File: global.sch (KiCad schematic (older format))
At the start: 37 parts, among them Q101 MMBT3904, U101 74HCT125, U102 74HC595, U103 74HC595, U104 74HC595, U105 74HC165

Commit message: renumbered pcb
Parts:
- renumbered C102 to C44, C103 to C45, C104 to C46, C105 to C50, C101 to C6, ENC101 to ENC1, JP101 to JP1, JP103 to JP2, JP102 to JP3, Q101 to Q5, R116 to R10, R117 to R11, R122 to R34, R105 to R47, R101 to R48, R102 to R53, R103 to R56, R104 to R59, R120 to R64, R118 to R65, R121 to R67, R113 to R68, R112 to R69, R119 to R7, R111 to R70, R110 to R71, R109 to R72, R108 to R73, R107 to R74, R106 to R75, R114 to R8, R115 to R9, U105 to U11, U102 to U12, U103 to U13, U104 to U14, U101 to U5
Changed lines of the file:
@@
 $EndDescr
 $Comp
-L ALPS-STEC12E08 ENC101
+L ALPS-STEC12E08 ENC1
 U 1 1 59AC9C93
 P 3050 6850
-F 0 "ENC101" H 3050 6500 50  0000 C CNN
+F 0 "ENC1" H 3050 6500 50  0000 C CNN
 F 1 "ALPS-STEC12E08" H 3050 7200 50  0000 C CNN
 F 2 "w_rotary_encoder:ALPS_STEC12E08" H 3050 6850 60  0001 C CNN
@@
 $EndComp
 $Comp
-L 74HC165 U105
+L 74HC165 U11
 U 1 1 59D8CB67
 P 5500 5100
-F 0 "U105" H 6000 4250 60  0000 C CNN
+F 0 "U11" H 6000 4250 60  0000 C CNN
 F 1 "74HC165" H 6000 5250 60  0000 C CNN
 F 2 "Housings_SOIC:SOIC-16_3.9x9.9mm_Pitch1.27mm" H 5500 5100 60  0001 C CNN
@@
 $EndComp
 $Comp
-L 74HC595 U102
+L 74HC595 U12
 U 1 1 59D8CB9A
 P 5500 900
-F 0 "U102" H 6000 50  60  0000 C CNN
+F 0 "U12" H 6000 50  60  0000 C CNN
 F 1 "74HC595" H 6000 1050 60  0000 C CNN
 F 2 "Housings_SOIC:SOIC-16_3.9x9.9mm_Pitch1.27mm" H 5500 900 60  0001 C CNN
@@
 $EndComp
 $Comp
-L 74HC595 U103
+L 74HC595 U13
 U 1 1 59DABD8B
 P 5500 2300
-F 0 "U103" H 6000 1450 60  0000 C CNN
+F 0 "U13" H 6000 1450 60  0000 C CNN
 F 1 "74HC595" H 6000 2450 60  0000 C CNN
 F 2 "Housings_SOIC:SOIC-16_3.9x9.9mm_Pitch1.27mm" H 5500 2300 60  0001 C CNN
@@
 $EndComp
 $Comp
-L 74HC595 U104
+L 74HC595 U14
 U 1 1 59DABDC7
 P 5500 3700
-F 0 "U104" H 6000 2850 60  0000 C CNN
+F 0 "U14" H 6000 2850 60  0000 C CNN
 F 1 "74HC595" H 6000 3850 60  0000 C CNN
 F 2 "Housings_SOIC:SOIC-16_3.9x9.9mm_Pitch1.27mm" H 5500 3700 60  0001 C CNN
@@
 $EndComp
 $Comp
-L C C101
+L C C6
 U 1 1 59DAD327
 P 5000 6850
-F 0 "C101" H 5025 6950 50  0000 L CNN
+F 0 "C6" H 5025 6950 50  0000 L CNN
 F 1 "100n" H 5025 6750 50  0000 L CNN
 F 2 "w_capacitor:C_0603" H 5038 6700 50  0001 C CNN
@@
 $EndComp
 $Comp
-L C C102
+L C C44
 U 1 1 59DAD399
 P 5300 6850
-F 0 "C102" H 5325 6950 50  0000 L CNN
+F 0 "C44" H 5325 6950 50  0000 L CNN
 F 1 "100n" H 5325 6750 50  0000 L CNN
 F 2 "w_capacitor:C_0603" H 5338 6700 50  0001 C CNN
@@
 $EndComp
 $Comp
-L C C103
+L C C45
 U 1 1 59DAD3D5
 P 5600 6850
-F 0 "C103" H 5625 6950 50  0000 L CNN
+F 0 "C45" H 5625 6950 50  0000 L CNN
 F 1 "100n" H 5625 6750 50  0000 L CNN
 F 2 "w_capacitor:C_0603" H 5638 6700 50  0001 C CNN
@@
 $EndComp
 $Comp
-L C C104
+L C C46
 U 1 1 59DAD3DB
 P 5900 6850
-F 0 "C104" H 5925 6950 50  0000 L CNN
+F 0 "C46" H 5925 6950 50  0000 L CNN
 F 1 "100n" H 5925 6750 50  0000 L CNN
 F 2 "w_capacitor:C_0603" H 5938 6700 50  0001 C CNN
@@
 $EndComp
 $Comp
-L C C105
+L C C50
 U 1 1 59DB526D
 P 6200 6850
-F 0 "C105" H 6225 6950 50  0000 L CNN
+F 0 "C50" H 6225 6950 50  0000 L CNN
 F 1 "100n" H 6225 6750 50  0000 L CNN
 F 2 "w_capacitor:C_0603" H 6238 6700 50  0001 C CNN
@@
 $EndComp
 $Comp
-L NHD-3.12-25664UC JP102
+L NHD-3.12-25664UC JP3
 U 1 1 59DBF1B1
 P 3000 3800
-F 0 "JP102" H 3650 1750 60  0000 C CNN
+F 0 "JP3" H 3650 1750 60  0000 C CNN
 F 1 "NHD-3.12-25664UC" H 3650 3950 60  0000 C CNN
 F 2 "w_lcd:NHD-3.12-25664UC" H 3200 4000 60  0001 C CNN
@@
 $EndComp
 $Comp
-L Micro_SD_Card JP103
+L Micro_SD_Card JP2
 U 1 1 59DC0C9C
 P 10100 1600
-F 0 "JP103" H 9450 2200 50  0000 C CNN
+F 0 "JP2" H 9450 2200 50  0000 C CNN
 F 1 "PJS008U-3000" H 10750 2200 50  0000 R CNN
 F 2 "w_connector:PJS008U-3000-0" H 11250 1900 50  0001 C CNN
@@
 $EndComp
 $Comp
-L USB_A JP101
+L USB_A JP1
 U 1 1 59DE5EB2
 P 10000 5600
-F 0 "JP101" H 9800 6050 50  0000 L CNN
+F 0 "JP1" H 9800 6050 50  0000 L CNN
 F 1 "USB_A" H 9800 5950 50  0000 L CNN
 F 2 "w_connector:MOLEX_USB_105057" H 10150 5550 50  0001 C CNN
@@
 $EndComp
 $Comp
-L R R101
+L R R48
 U 1 1 59E55F0E
 P 6700 4950
-F 0 "R101" V 6650 5100 50  0000 L CNN
+F 0 "R48" V 6650 5100 50  0000 L CNN
 F 1 "10k" V 6700 4950 50  0000 C CNN
 F 2 "w_resistor:R_0603" V 6630 4950 50  0001 C CNN
@@
 $EndComp
 $Comp
-L R R102
+L R R53
 U 1 1 59E560D3
 P 6800 4950
-F 0 "R102" V 6750 5100 50  0000 L CNN
+F 0 "R53" V 6750 5100 50  0000 L CNN
 F 1 "10k" V 6800 4950 50  0000 C CNN
 F 2 "w_resistor:R_0603" V 6730 4950 50  0001 C CNN
@@
 $EndComp
 $Comp
-L R R103
+L R R56
 U 1 1 59E56118
 P 6900 4950
-F 0 "R103" V 6850 5100 50  0000 L CNN
+F 0 "R56" V 6850 5100 50  0000 L CNN
 F 1 "10k" V 6900 4950 50  0000 C CNN
 F 2 "w_resistor:R_0603" V 6830 4950 50  0001 C CNN
@@
 $EndComp
 $Comp
-L R R104
+L R R59
 U 1 1 59E56160
 P 7000 4950
-F 0 "R104" V 6950 5100 50  0000 L CNN
+F 0 "R59" V 6950 5100 50  0000 L CNN
 F 1 "10k" V 7000 4950 50  0000 C CNN
 F 2 "w_resistor:R_0603" V 6930 4950 50  0001 C CNN
@@
 $EndComp
 $Comp
-L R R105
+L R R47
 U 1 1 59E561AB
 P 7100 4950
-F 0 "R105" V 7050 5100 50  0000 L CNN
+F 0 "R47" V 7050 5100 50  0000 L CNN
 F 1 "10k" V 7100 4950 50  0000 C CNN
 F 2 "w_resistor:R_0603" V 7030 4950 50  0001 C CNN
@@
 $EndComp
 $Comp
-L R R107
+L R R74
 U 1 1 59E604C8
 P 6750 2400
-F 0 "R107" V 6700 2550 50  0000 L CNN
+F 0 "R74" V 6700 2550 50  0000 L CNN
 F 1 "470" V 6750 2400 50  0000 C CNN
 F 2 "w_resistor:R_0603" V 6680 2400 50  0001 C CNN
@@
 $EndComp
 $Comp
-L R R106
+L R R75
 U 1 1 59E60528
 P 6750 2300
-F 0 "R106" V 6700 2450 50  0000 L CNN
+F 0 "R75" V 6700 2450 50  0000 L CNN
 F 1 "470" V 6750 2300 50  0000 C CNN
 F 2 "w_resistor:R_0603" V 6680 2300 50  0001 C CNN
@@
 $EndComp
 $Comp
-L R R108
+L R R73
 U 1 1 59E60C94
 P 6750 2500
-F 0 "R108" V 6700 2650 50  0000 L CNN
+F 0 "R73" V 6700 2650 50  0000 L CNN
 F 1 "470" V 6750 2500 50  0000 C CNN
 F 2 "w_resistor:R_0603" V 6680 2500 50  0001 C CNN
@@
 $EndComp
 $Comp
-L R R109
+L R R72
 U 1 1 59E60F5A
 P 6750 2600
-F 0 "R109" V 6700 2750 50  0000 L CNN
+F 0 "R72" V 6700 2750 50  0000 L CNN
 F 1 "470" V 6750 2600 50  0000 C CNN
 F 2 "w_resistor:R_0603" V 6680 2600 50  0001 C CNN
@@
 $EndComp
 $Comp
-L R R113
+L R R68
 U 1 1 59E61471
 P 6750 3000
-F 0 "R113" V 6700 3150 50  0000 L CNN
+F 0 "R68" V 6700 3150 50  0000 L CNN
 F 1 "470" V 6750 3000 50  0000 C CNN
 F 2 "w_resistor:R_0603" V 6680 3000 50  0001 C CNN
@@
 $EndComp
 $Comp
-L R R112
+L R R69
 U 1 1 59E6153A
 P 6750 2900
-F 0 "R112" V 6700 3050 50  0000 L CNN
+F 0 "R69" V 6700 3050 50  0000 L CNN
 F 1 "470" V 6750 2900 50  0000 C CNN
 F 2 "w_resistor:R_0603" V 6680 2900 50  0001 C CNN
@@
 $EndComp
 $Comp
-L R R111
+L R R70
 U 1 1 59E61584
 P 6750 2800
-F 0 "R111" V 6700 2950 50  0000 L CNN
+F 0 "R70" V 6700 2950 50  0000 L CNN
 F 1 "470" V 6750 2800 50  0000 C CNN
 F 2 "w_resistor:R_0603" V 6680 2800 50  0001 C CNN
@@
 $EndComp
 $Comp
-L R R110
+L R R71
 U 1 1 59E6158A
 P 6750 2700
-F 0 "R110" V 6700 2850 50  0000 L CNN
+F 0 "R71" V 6700 2850 50  0000 L CNN
 F 1 "470" V 6750 2700 50  0000 C CNN
 F 2 "w_resistor:R_0603" V 6680 2700 50  0001 C CNN
@@
 $EndComp
 $Comp
-L 74HCT125 U101
+L 74HCT125 U5
 U 1 1 59E5EC51
 P 3000 800
-F 0 "U101" H 3500 -250 60  0000 C CNN
+F 0 "U5" H 3500 -250 60  0000 C CNN
 F 1 "74HCT125" H 3500 950 60  0000 C CNN
 F 2 "Housings_SOIC:SOIC-14_3.9x8.7mm_Pitch1.27mm" H 3450 900 60  0001 C CNN
@@
 $EndComp
 $Comp
-L R R117
+L R R11
 U 1 1 5AEA4C2A
 P 8900 1050
-F 0 "R117" V 8980 1050 50  0000 C CNN
+F 0 "R11" V 8980 1050 50  0000 C CNN
 F 1 "33k" V 8900 1050 50  0000 C CNN
 F 2 "w_resistor:R_0603" V 8830 1050 50  0001 C CNN
@@
 $EndComp
 $Comp
-L R R119
+L R R7
 U 1 1 5AEA4CDA
 P 8900 2250
-F 0 "R119" V 8980 2250 50  0000 C CNN
+F 0 "R7" V 8980 2250 50  0000 C CNN
 F 1 "1M" V 8900 2250 50  0000 C CNN
 F 2 "w_resistor:R_0603" V 8830 2250 50  0001 C CNN
@@
 $EndComp
 $Comp
-L R R114
+L R R8
 U 1 1 5AEA4D5E
 P 8300 1050
-F 0 "R114" V 8380 1050 50  0000 C CNN
+F 0 "R8" V 8380 1050 50  0000 C CNN
 F 1 "33k" V 8300 1050 50  0000 C CNN
 F 2 "w_resistor:R_0603" V 8230 1050 50  0001 C CNN
@@
 $EndComp
 $Comp
-L R R115
+L R R9
 U 1 1 5AEA4DC8
 P 8500 1050
-F 0 "R115" V 8580 1050 50  0000 C CNN
+F 0 "R9" V 8580 1050 50  0000 C CNN
 F 1 "33k" V 8500 1050 50  0000 C CNN
 F 2 "w_resistor:R_0603" V 8430 1050 50  0001 C CNN
@@
 $EndComp
 $Comp
-L R R116
+L R R10
 U 1 1 5AEA93F2
 P 8700 1050
-F 0 "R116" V 8780 1050 50  0000 C CNN
+F 0 "R10" V 8780 1050 50  0000 C CNN
 F 1 "33k" V 8700 1050 50  0000 C CNN
 F 2 "w_resistor:R_0603" V 8630 1050 50  0001 C CNN
@@
 $EndComp
 $Comp
-L R R122
+L R R34
 U 1 1 5AEB2AD1
 P 2700 5650
-F 0 "R122" V 2780 5650 50  0000 C CNN
+F 0 "R34" V 2780 5650 50  0000 C CNN
 F 1 "10k" V 2700 5650 50  0000 C CNN
 F 2 "w_resistor:R_0603" V 2630 5650 50  0001 C CNN
@@
 $EndComp
 $Comp
-L MMBT3904 Q101
+L MMBT3904 Q5
 U 1 1 5AEB9A70
 P 4000 2700
-F 0 "Q101" H 4200 2775 50  0000 L CNN
+F 0 "Q5" H 4200 2775 50  0000 L CNN
 F 1 "MMBT3904" H 4200 2700 50  0000 L CNN
 F 2 "TO_SOT_Packages_SMD:SOT-23" H 4200 2625 50  0001 L CIN
@@
 $EndComp
 $Comp
-L R R118
+L R R65
 U 1 1 5AEB9A79
 P 4100 2150
-F 0 "R118" V 4180 2150 50  0000 C CNN
+F 0 "R65" V 4180 2150 50  0000 C CNN
 F 1 "1k" V 4100 2150 50  0000 C CNN
 F 2 "w_resistor:R_0603" V 4030 2150 50  0001 C CNN
@@
 $EndComp
 $Comp
-L R R120
+L R R64
 U 1 1 5AEBCC66
 P 3450 2700
-F 0 "R120" V 3530 2700 50  0000 C CNN
+F 0 "R64" V 3530 2700 50  0000 C CNN
 F 1 "10k" V 3450 2700 50  0000 C CNN
 F 2 "w_resistor:R_0603" V 3380 2700 50  0001 C CNN
@@
 $EndComp
 $Comp
-L R R121
+L R R67
 U 1 1 5AEBCE61
 P 3700 2950
-F 0 "R121" V 3780 2950 50  0000 C CNN
+F 0 "R67" V 3780 2950 50  0000 C CNN
 F 1 "100k" V 3700 2950 50  0000 C CNN
 F 2 "w_resistor:R_0603" V 3630 2950 50  0001 C CNN

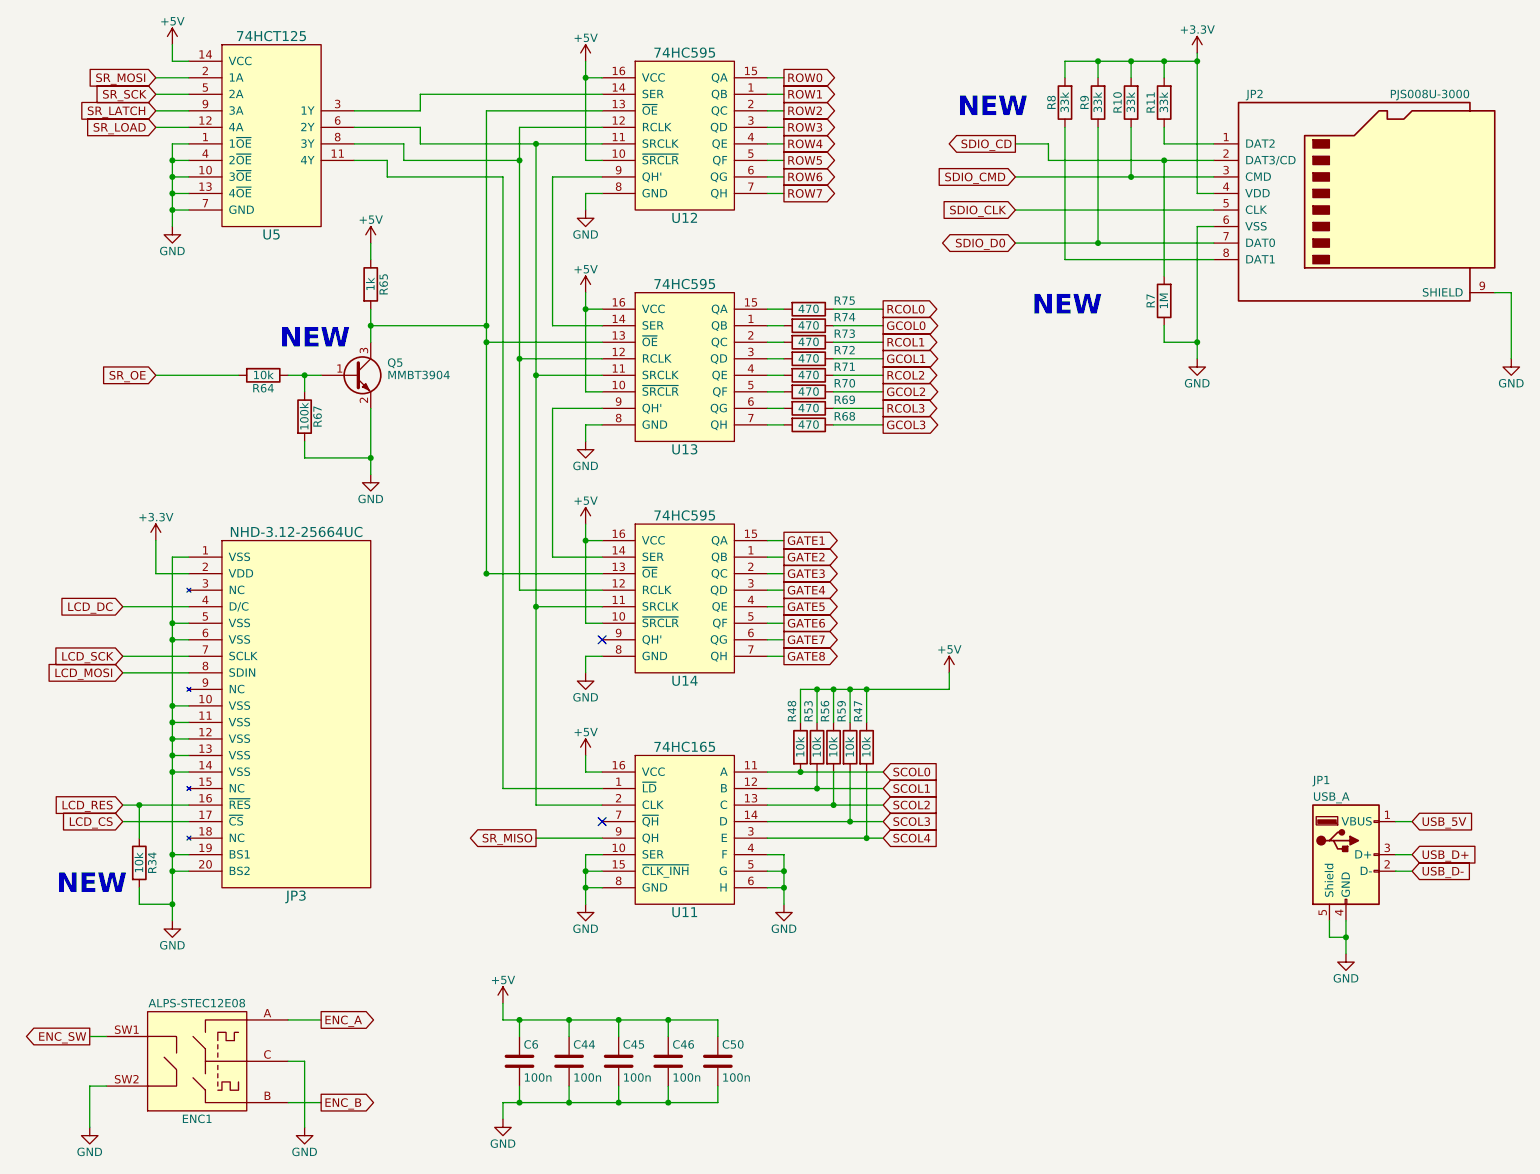
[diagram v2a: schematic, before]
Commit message: corrected some part values
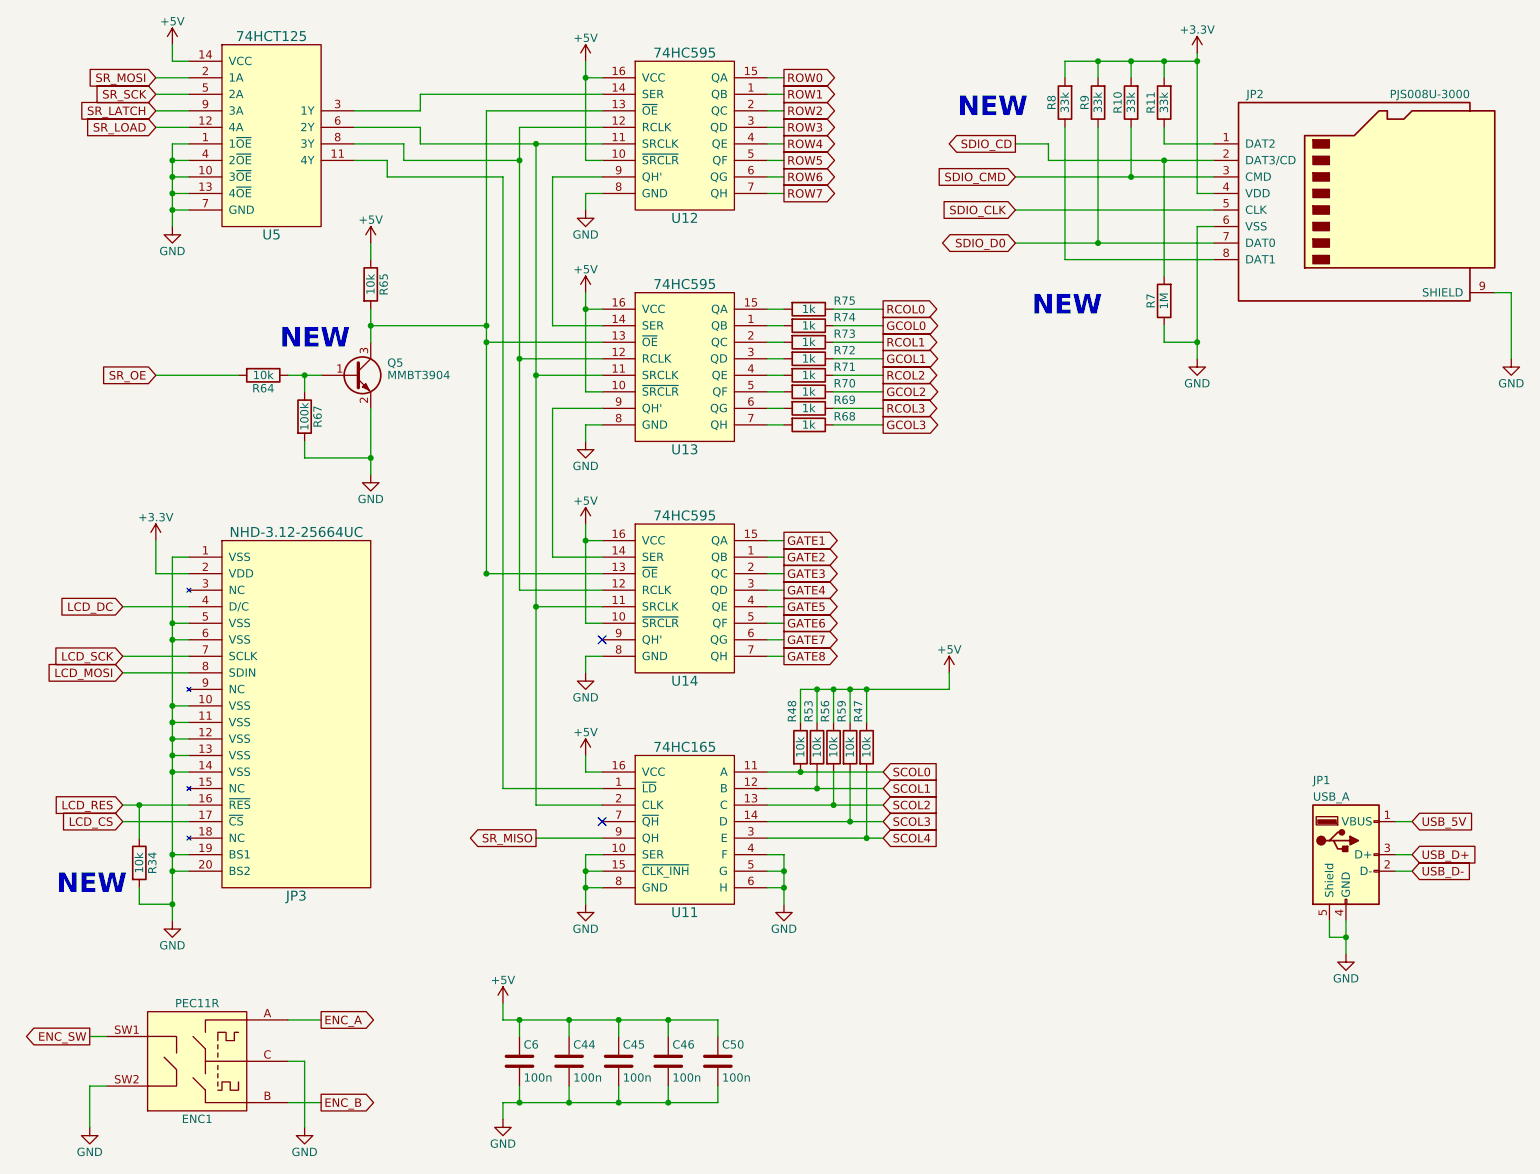
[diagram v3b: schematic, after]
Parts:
- ENC1: value ALPS-STEC12E08 -> PEC11R; MFP PEC11R-4225F-S0024 -> PEC11R-4220F-S0024
- R65: value 1k -> 10k; MFP ERJ-3EKF1001V -> ERJ-3EKF1002V
- R68, R69, R70, R71, R72, R73, R74, R75: value 470 -> 1k; MFP ERJ-3EKF4700V -> ERJ-3EKF1001V
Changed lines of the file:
@@
 P 3050 6850
 F 0 "ENC1" H 3050 6500 50  0000 C CNN
-F 1 "ALPS-STEC12E08" H 3050 7200 50  0000 C CNN
+F 1 "PEC11R" H 3050 7200 50  0000 C CNN
 F 2 "w_rotary_encoder:ALPS_STEC12E08" H 3050 6850 60  0001 C CNN
-F 3 "http://datasheet.octopart.com/PEC11R-4225F-S0024-Bourns-datasheet-68303416.pdf" H 3050 6850 60  0001 C CNN
+F 3 "http://datasheet.octopart.com/PEC11R-4220F-S0024-Bourns-datasheet-68303416.pdf" H 3050 6850 60  0001 C CNN
 F 4 "Bourns" H 3050 6600 50  0001 C CNN "MFN"
-F 5 "PEC11R-4225F-S0024" H 3050 6600 50  0001 C CNN "MFP"
+F 5 "PEC11R-4220F-S0024" H 3050 6600 50  0001 C CNN "MFP"
 	1    3050 6850
 	1    0    0    -1
@@
 P 6750 2400
 F 0 "R74" V 6700 2550 50  0000 L CNN
-F 1 "470" V 6750 2400 50  0000 C CNN
+F 1 "1k" V 6750 2400 50  0000 C CNN
 F 2 "w_resistor:R_0603" V 6680 2400 50  0001 C CNN
-F 3 "http://datasheet.octopart.com/ERJ3EKF4700V-Panasonic-datasheet-13266541.pdf" H 6750 2400 50  0001 C CNN
+F 3 "http://datasheet.octopart.com/ERJ-3EKF1001V-Panasonic-datasheet-82288794.pdf" H 6750 2400 50  0001 C CNN
 F 4 "Panasonic" H 6700 2650 50  0001 C CNN "MFN"
-F 5 "ERJ-3EKF4700V" H 6700 2650 50  0001 C CNN "MFP"
+F 5 "ERJ-3EKF1001V" H 6700 2650 50  0001 C CNN "MFP"
 	1    6750 2400
 	0    1    1    0
@@
 P 6750 2300
 F 0 "R75" V 6700 2450 50  0000 L CNN
-F 1 "470" V 6750 2300 50  0000 C CNN
+F 1 "1k" V 6750 2300 50  0000 C CNN
 F 2 "w_resistor:R_0603" V 6680 2300 50  0001 C CNN
-F 3 "http://datasheet.octopart.com/ERJ3EKF4700V-Panasonic-datasheet-13266541.pdf" H 6750 2300 50  0001 C CNN
+F 3 "http://datasheet.octopart.com/ERJ-3EKF1001V-Panasonic-datasheet-82288794.pdf" H 6750 2300 50  0001 C CNN
 F 4 "Panasonic" H 6700 2550 50  0001 C CNN "MFN"
-F 5 "ERJ-3EKF4700V" H 6700 2550 50  0001 C CNN "MFP"
+F 5 "ERJ-3EKF1001V" H 6700 2550 50  0001 C CNN "MFP"
 	1    6750 2300
 	0    1    1    0
@@
 P 6750 2500
 F 0 "R73" V 6700 2650 50  0000 L CNN
-F 1 "470" V 6750 2500 50  0000 C CNN
+F 1 "1k" V 6750 2500 50  0000 C CNN
 F 2 "w_resistor:R_0603" V 6680 2500 50  0001 C CNN
-F 3 "http://datasheet.octopart.com/ERJ3EKF4700V-Panasonic-datasheet-13266541.pdf" H 6750 2500 50  0001 C CNN
+F 3 "http://datasheet.octopart.com/ERJ-3EKF1001V-Panasonic-datasheet-82288794.pdf" H 6750 2500 50  0001 C CNN
 F 4 "Panasonic" H 6700 2750 50  0001 C CNN "MFN"
-F 5 "ERJ-3EKF4700V" H 6700 2750 50  0001 C CNN "MFP"
+F 5 "ERJ-3EKF1001V" H 6700 2750 50  0001 C CNN "MFP"
 	1    6750 2500
 	0    1    1    0
@@
 P 6750 2600
 F 0 "R72" V 6700 2750 50  0000 L CNN
-F 1 "470" V 6750 2600 50  0000 C CNN
+F 1 "1k" V 6750 2600 50  0000 C CNN
 F 2 "w_resistor:R_0603" V 6680 2600 50  0001 C CNN
-F 3 "http://datasheet.octopart.com/ERJ3EKF4700V-Panasonic-datasheet-13266541.pdf" H 6750 2600 50  0001 C CNN
+F 3 "http://datasheet.octopart.com/ERJ-3EKF1001V-Panasonic-datasheet-82288794.pdf" H 6750 2600 50  0001 C CNN
 F 4 "Panasonic" H 6700 2850 50  0001 C CNN "MFN"
-F 5 "ERJ-3EKF4700V" H 6700 2850 50  0001 C CNN "MFP"
+F 5 "ERJ-3EKF1001V" H 6700 2850 50  0001 C CNN "MFP"
 	1    6750 2600
 	0    1    1    0
@@
 P 6750 3000
 F 0 "R68" V 6700 3150 50  0000 L CNN
-F 1 "470" V 6750 3000 50  0000 C CNN
+F 1 "1k" V 6750 3000 50  0000 C CNN
 F 2 "w_resistor:R_0603" V 6680 3000 50  0001 C CNN
-F 3 "http://datasheet.octopart.com/ERJ3EKF4700V-Panasonic-datasheet-13266541.pdf" H 6750 3000 50  0001 C CNN
+F 3 "http://datasheet.octopart.com/ERJ-3EKF1001V-Panasonic-datasheet-82288794.pdf" H 6750 3000 50  0001 C CNN
 F 4 "Panasonic" H 6700 3250 50  0001 C CNN "MFN"
-F 5 "ERJ-3EKF4700V" H 6700 3250 50  0001 C CNN "MFP"
+F 5 "ERJ-3EKF1001V" H 6700 3250 50  0001 C CNN "MFP"
 	1    6750 3000
 	0    1    1    0
@@
 P 6750 2900
 F 0 "R69" V 6700 3050 50  0000 L CNN
-F 1 "470" V 6750 2900 50  0000 C CNN
+F 1 "1k" V 6750 2900 50  0000 C CNN
 F 2 "w_resistor:R_0603" V 6680 2900 50  0001 C CNN
-F 3 "http://datasheet.octopart.com/ERJ3EKF4700V-Panasonic-datasheet-13266541.pdf" H 6750 2900 50  0001 C CNN
+F 3 "http://datasheet.octopart.com/ERJ-3EKF1001V-Panasonic-datasheet-82288794.pdf" H 6750 2900 50  0001 C CNN
 F 4 "Panasonic" H 6700 3150 50  0001 C CNN "MFN"
-F 5 "ERJ-3EKF4700V" H 6700 3150 50  0001 C CNN "MFP"
+F 5 "ERJ-3EKF1001V" H 6700 3150 50  0001 C CNN "MFP"
 	1    6750 2900
 	0    1    1    0
@@
 P 6750 2800
 F 0 "R70" V 6700 2950 50  0000 L CNN
-F 1 "470" V 6750 2800 50  0000 C CNN
+F 1 "1k" V 6750 2800 50  0000 C CNN
 F 2 "w_resistor:R_0603" V 6680 2800 50  0001 C CNN
-F 3 "http://datasheet.octopart.com/ERJ3EKF4700V-Panasonic-datasheet-13266541.pdf" H 6750 2800 50  0001 C CNN
+F 3 "http://datasheet.octopart.com/ERJ-3EKF1001V-Panasonic-datasheet-82288794.pdf" H 6750 2800 50  0001 C CNN
 F 4 "Panasonic" H 6700 3050 50  0001 C CNN "MFN"
-F 5 "ERJ-3EKF4700V" H 6700 3050 50  0001 C CNN "MFP"
+F 5 "ERJ-3EKF1001V" H 6700 3050 50  0001 C CNN "MFP"
 	1    6750 2800
 	0    1    1    0
@@
 P 6750 2700
 F 0 "R71" V 6700 2850 50  0000 L CNN
-F 1 "470" V 6750 2700 50  0000 C CNN
+F 1 "1k" V 6750 2700 50  0000 C CNN
 F 2 "w_resistor:R_0603" V 6680 2700 50  0001 C CNN
-F 3 "http://datasheet.octopart.com/ERJ3EKF4700V-Panasonic-datasheet-13266541.pdf" H 6750 2700 50  0001 C CNN
+F 3 "http://datasheet.octopart.com/ERJ-3EKF1001V-Panasonic-datasheet-82288794.pdf" H 6750 2700 50  0001 C CNN
 F 4 "Panasonic" H 6700 2950 50  0001 C CNN "MFN"
-F 5 "ERJ-3EKF4700V" H 6700 2950 50  0001 C CNN "MFP"
+F 5 "ERJ-3EKF1001V" H 6700 2950 50  0001 C CNN "MFP"
 	1    6750 2700
 	0    1    1    0
@@
 P 4100 2150
 F 0 "R65" V 4180 2150 50  0000 C CNN
-F 1 "1k" V 4100 2150 50  0000 C CNN
+F 1 "10k" V 4100 2150 50  0000 C CNN
 F 2 "w_resistor:R_0603" V 4030 2150 50  0001 C CNN
-F 3 "http://datasheet.octopart.com/ERJ-3EKF1001V-Panasonic-datasheet-82288794.pdf" H 4100 2150 50  0001 C CNN
+F 3 "http://datasheet.octopart.com/ERJ-3EKF1002V-Panasonic-datasheet-13266541.pdf" H 4100 2150 50  0001 C CNN
 F 4 "Panasonic" H 4180 2250 50  0001 C CNN "MFN"
-F 5 "ERJ-3EKF1001V" H 4180 2250 50  0001 C CNN "MFP"
+F 5 "ERJ-3EKF1002V" H 4180 2250 50  0001 C CNN "MFP"
 	1    4100 2150
 	1    0    0    -1
